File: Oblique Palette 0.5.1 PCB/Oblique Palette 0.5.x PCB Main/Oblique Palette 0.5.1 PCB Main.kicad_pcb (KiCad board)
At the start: 2 copper layers, 235 x 110 mm, 309 parts, among them J11 Conn_01x03_Male_Pin, J13 Conn_01x03_Male_Pin, J14 Conn_01x03_Male_Pin, J16 Conn_01x03_Female_Pin, J17 AudioJack2_SwitchT, J19 Conn_01x03_Female_Pin, J2 Conn_01x03_Male_Pin, J20 AudioJack2_SwitchT, J22 Conn_01x03_Female_Pin, J23 AudioJack2_SwitchT, J25 Conn_01x03_Female_Pin, J26 AudioJack2_SwitchT, J28 Conn_01x03_Female_Pin, J29 AudioJack2_SwitchT, J31 Conn_01x03_Female_Pin, J32 AudioJack2_SwitchT, J34 Conn_01x03_Female_Pin, J35 AudioJack2_SwitchT, J37 Conn_01x03_Female_Pin, J38 AudioJack2_SwitchT, J4 Conn_01x03_Male_Pin, J40 Conn_01x03_Female_Pin, J42 AudioJack2_SwitchT, J44 Conn_01x03_Female_Pin, J46 AudioJack2_SwitchT, J48 Conn_01x03_Female_Pin, J5 Conn_01x03_Male_Pin, J50 AudioJack2_SwitchT, J52 Conn_01x03_Female_Pin, J54 AudioJack2_SwitchT, J56 Conn_01x03_Female_Pin, J58 AudioJack2_SwitchT, J60 Conn_01x03_Female_Pin, J62 AudioJack2_SwitchT, J64 Conn_01x03_Female_Pin, J66 AudioJack2_SwitchT, J68 Conn_01x03_Female_Pin, J7 Conn_01x03_Male_Pin, J70 AudioJack2_SwitchT, J72 Conn_01x02_Pin, J9 Conn_01x03_Male_Pin, U1 CD4051B, U10 MCP6004, U11 MCP4725xxx-xCH, U12 MCP6004, U13 MCP4725xxx-xCH, U14 MCP6004, U15 MCP4725xxx-xCH, U16 MCP6004, U17 MCP4725xxx-xCH, U18 MCP6004, U19 MCP4725xxx-xCH, U2 Pico, U20 MCP6004, U21 MCP4725xxx-xCH, U22 MCP6004, U23 MCP4725xxx-xCH, U24 MCP6004, U25 MCP4725xxx-xCH, U26 MCP6004, U3 MCP6004, U4 MCP6004, U5 MCP6004, U6 MCP6004, U7 MCP6004, U8 MCP6004, U9 MCP6004

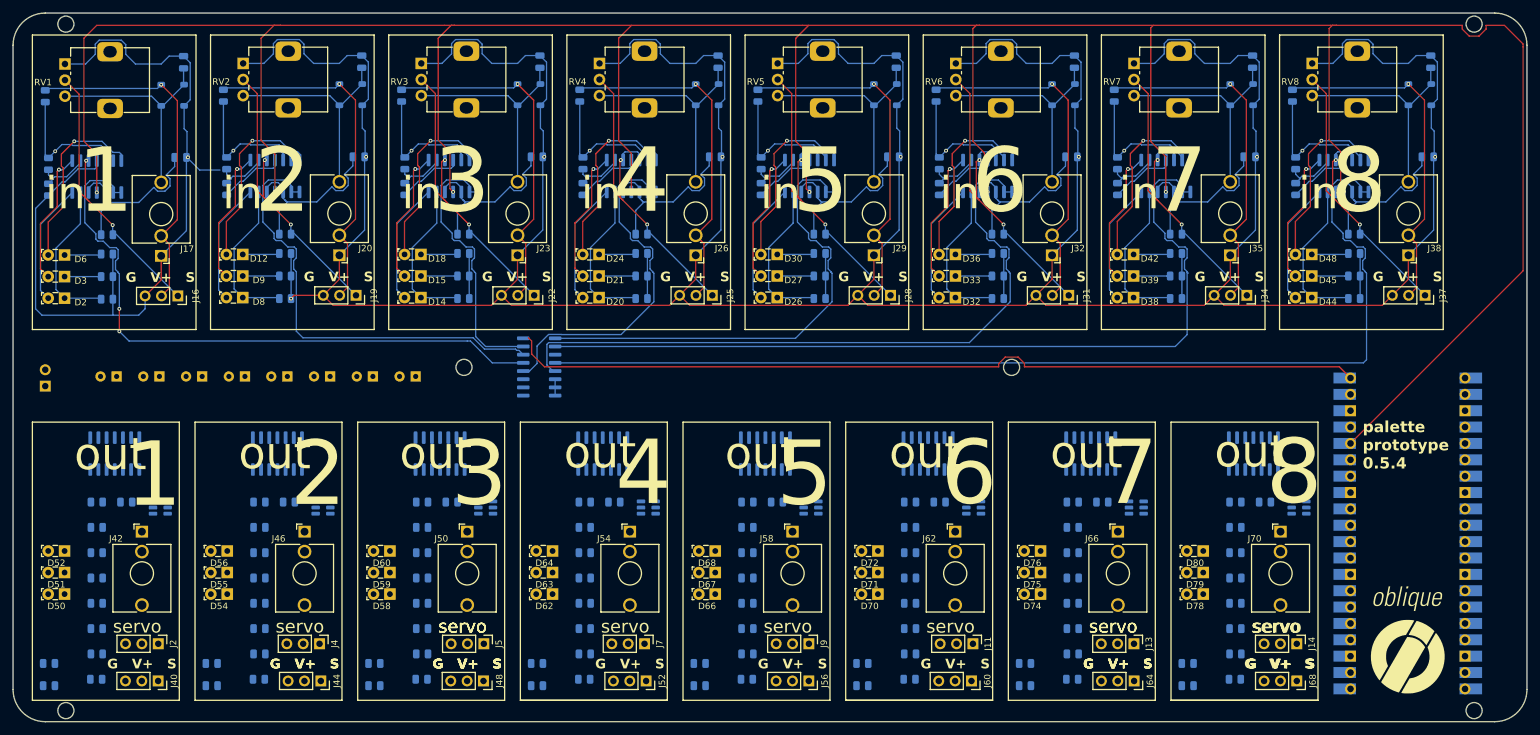
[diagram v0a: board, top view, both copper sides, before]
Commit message: All traces connected. Replaced caps with 1mF SMD ones to add muffling power for and to the servos.
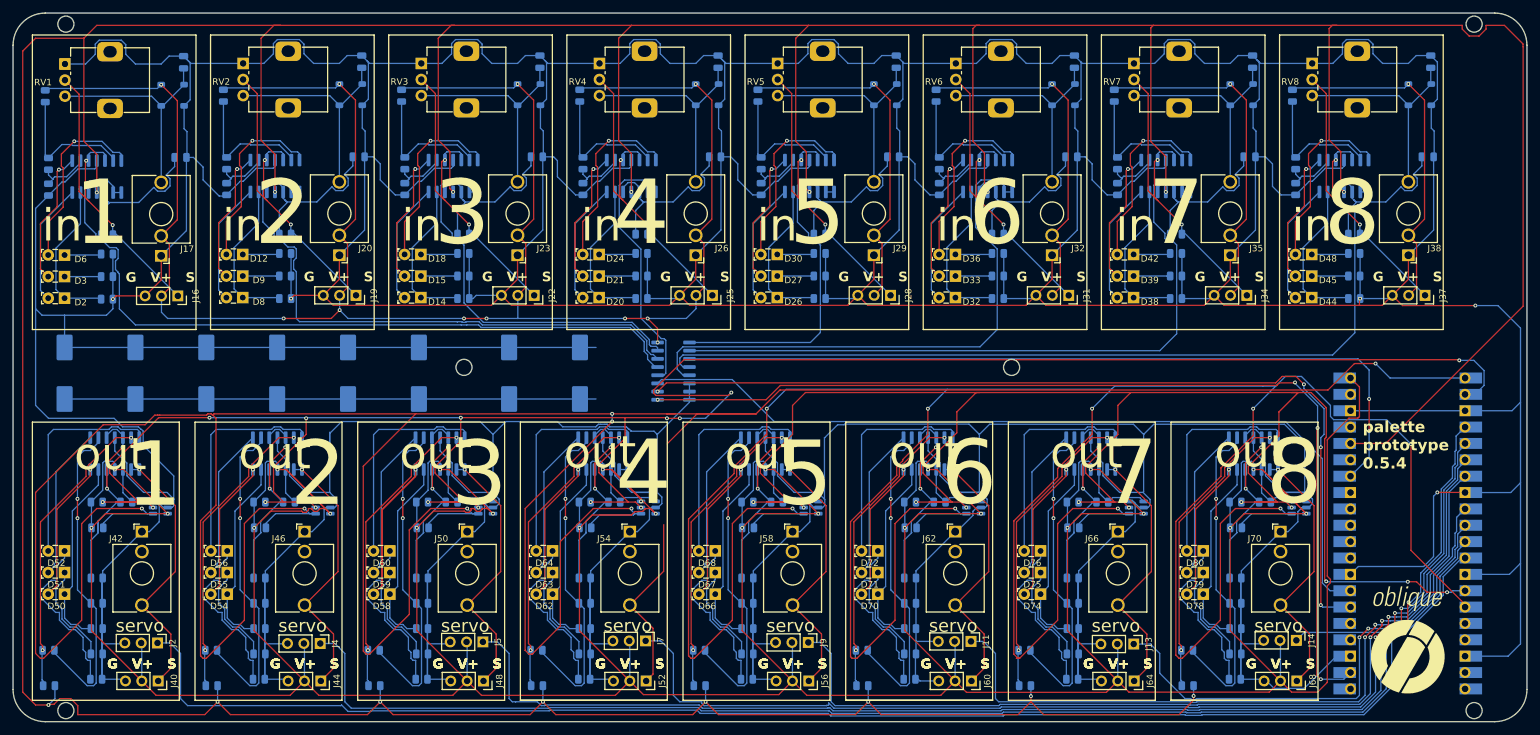
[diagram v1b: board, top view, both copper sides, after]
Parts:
- removed J72: Conn_01x02_Pin, Connector_PinHeader_2.54mm:PinHeader_1x02_P2.54mm_Vertical
- removed R110, R121, R132, R143, R66, R77, R88, R99: 100K, Resistor_SMD:R_0805_2012Metric
- C1, C2, C3, C4, C5, C6, C7, C8: value 100uF -> 1mF; footprint Capacitor_THT:CP_Radial_D5.0mm_P2.50mm -> Capacitor_SMD:CP_Elec_10x10
- moved C1 25.5 mm to (103.0, 72.4), turned to 90 degrees
- moved C3 21.1 mm to (92.0, 72.4), turned to 90 degrees
- moved U1 20.9 mm to (117.5, 72.1)
- moved C5 13.8 mm to (78.0, 72.4), turned to 90 degrees
- moved C7 9.43 mm to (67.0, 72.4), turned to 90 degrees
- moved C8 8.10 mm to (23.0, 72.4), turned to 90 degrees
- moved C2 5.02 mm to (56.0, 72.4), turned to 90 degrees
- moved R100 3.86 mm to (103.8, 96.4)
- moved R111 3.86 mm to (129.1, 96.4)
- moved R122 3.86 mm to (154.3, 96.4)
- moved R133 3.86 mm to (179.6, 96.4)
- moved R144 3.86 mm to (204.8, 96.4)
- moved R67 3.86 mm to (28.1, 96.4)
- moved R78 3.86 mm to (53.3, 96.4)
- moved R89 3.86 mm to (78.6, 96.4)
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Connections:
- net V_SERVO renamed VCC
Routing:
- net GNDREF: track 880.1 -> 2119.0 mm, vias 9 -> 5
- net VCC: track 567.4 -> 1455.0 mm, vias 8 -> 42
- net SDA_0: track 0.00 -> 574.2 mm, vias 0 -> 7
- net SCL_1: track 0.00 -> 506.8 mm, vias 0 -> 9
- net SCL_0: track 0.00 -> 347.7 mm, vias 0 -> 15
- net +3.3V: track 519.4 -> 848.8 mm, vias 8 -> 16
- net SDA_1: track 0.00 -> 267.4 mm, vias 0 -> 11
- net SERVO_1: track 0.00 -> 247.8 mm, vias 0 -> 2
- net SERVO_2: track 0.00 -> 219.7 mm, vias 0 -> 2
- net SERVO_3: track 0.00 -> 191.5 mm, vias 0 -> 2
- net SERVO_4: track 0.00 -> 164.3 mm, vias 0 -> 2
- net Net-(U1-C): track 0.00 -> 152.9 mm, vias 0 -> 4
- net Net-(U1-B): track 0.00 -> 142.3 mm, vias 0 -> 4
- net SERVO_5: track 0.00 -> 133.6 mm, vias 0 -> 2
- net Net-(U1-A): track 0.00 -> 132.7 mm
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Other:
- board text removed: "DAC Address Jumper Open, A0 = GND Closed A0 = V+"
- board text removed: "GND"
- board text removed: "V Ext"

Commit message: Ugh. Looks like the connections to VCC and GND of the power caps got deleted in the last second. Fixed now, will see if I need to bridge on 0.5.4
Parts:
- added G***: LOGO, LOGO, F.Cu at (231.5, 97.9)
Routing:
- net GNDREF: track 2119.0 -> 2153.2 mm
- net SDA_0: track 574.2 -> 559.5 mm
- net VCC: track 1455.0 -> 1468.9 mm, vias 42 -> 43
- net Net-(J52-Pin_1): track 29.6 -> 40.4 mm, vias 0 -> 1
- net /Input 8/ANALOG_CHANNEL: track 130.7 -> 140.4 mm
- net SCL_0: track 347.7 -> 340.3 mm, vias 15 -> 14
- net Net-(U1-X): track 123.9 -> 124.9 mm
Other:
- board text added: "palette prototype 0.5.5"
- board text removed: "V+"
- board text removed: "palette prototype 0.5.4"
